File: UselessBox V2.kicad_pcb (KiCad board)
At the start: 2 copper layers, 47.1 x 46.6 mm, 23 parts, among them J2 Conn_01x03, J3 Conn_01x02_Female, SW1 SW_SPDT, SW2 SW_SPDT, U1 L7805CV, U2 LM555CN_NOPB

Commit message: corrected power switch location
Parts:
- removed G***: LOGO, Kicad:TNT Logo 12.6mm x 7mm
- removed G***: LOGO, Kicad:TSL Technologies logo 16mm x 11mm
- R3: value 82KΩ -> 100KΩ
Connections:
- D5 pad 2: /5Vout -> /5V
- J2 pad 2: /5Vout -> /5V
- J3 pad 2: /B+ -> Net-(J3-Pad2)
- R2 pad 1: /5Vout -> /5V
- R3 pad 1: /5Vout -> /5V
- SW1 pad 1: /5Vout -> /B+
- SW1 pad 2: /5V -> Net-(J3-Pad2)
- U2 pad 4: /5Vout -> /5V
- U2 pad 8: /5Vout -> /5V
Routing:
- net /5Vout: track 157.8 -> 0.00 mm
- net /5V: track 51.6 -> 125.9 mm
- net Net-(J3-Pad2): track 0.00 -> 43.0 mm
- net /B+: track 33.0 -> 48.2 mm
- net /B-: track 38.4 -> 44.0 mm
- added copper zone on F.Cu, net /5V
- removed copper zone on F.Cu, net /5Vout

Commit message: stl file done for base and arm also revised PCB switch
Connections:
- net /5V renamed /5Vout
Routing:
- net /GND: track 16.4 -> 78.0 mm
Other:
- board text added: "Useless Box V2 Timothy S Leishman 4/25/2022"
- board text removed: "Useless Box V2 Timothy S Leishman 4/12/2022"

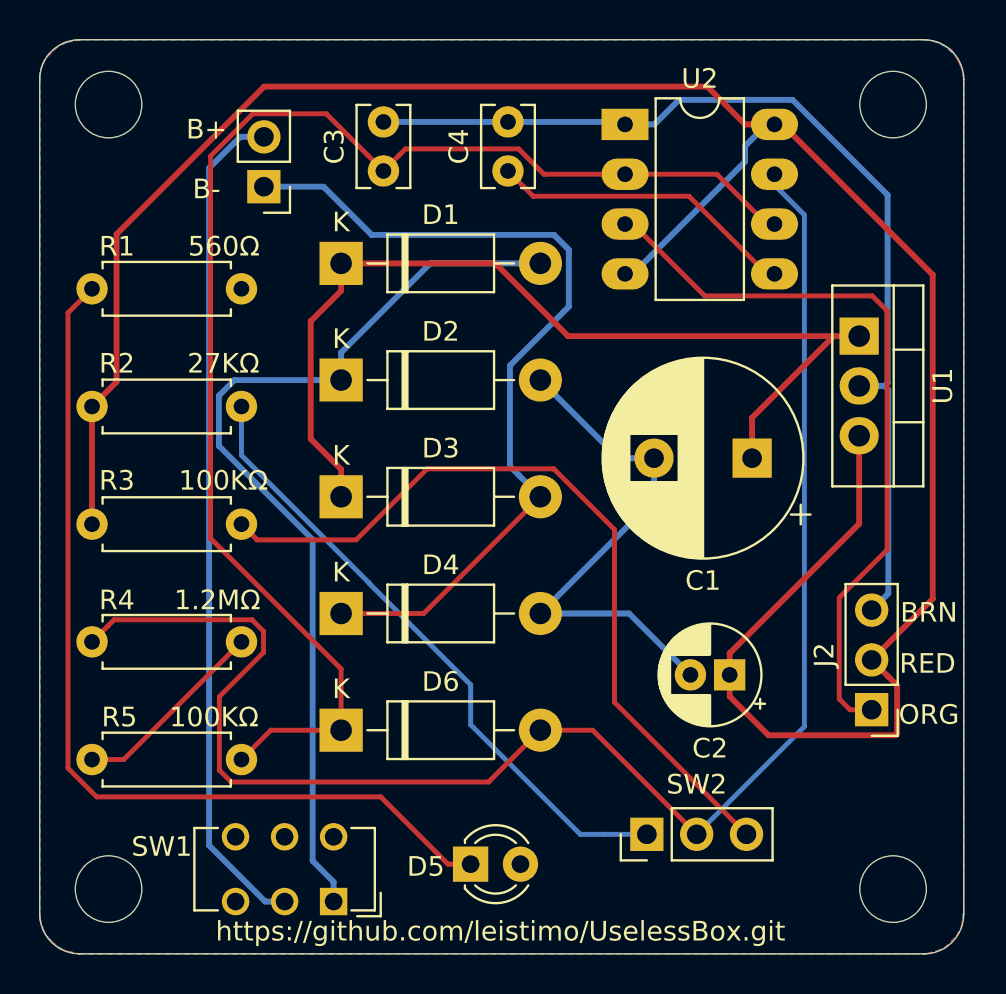
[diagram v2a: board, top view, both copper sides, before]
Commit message: Corrected ground problem and generated Gerbers
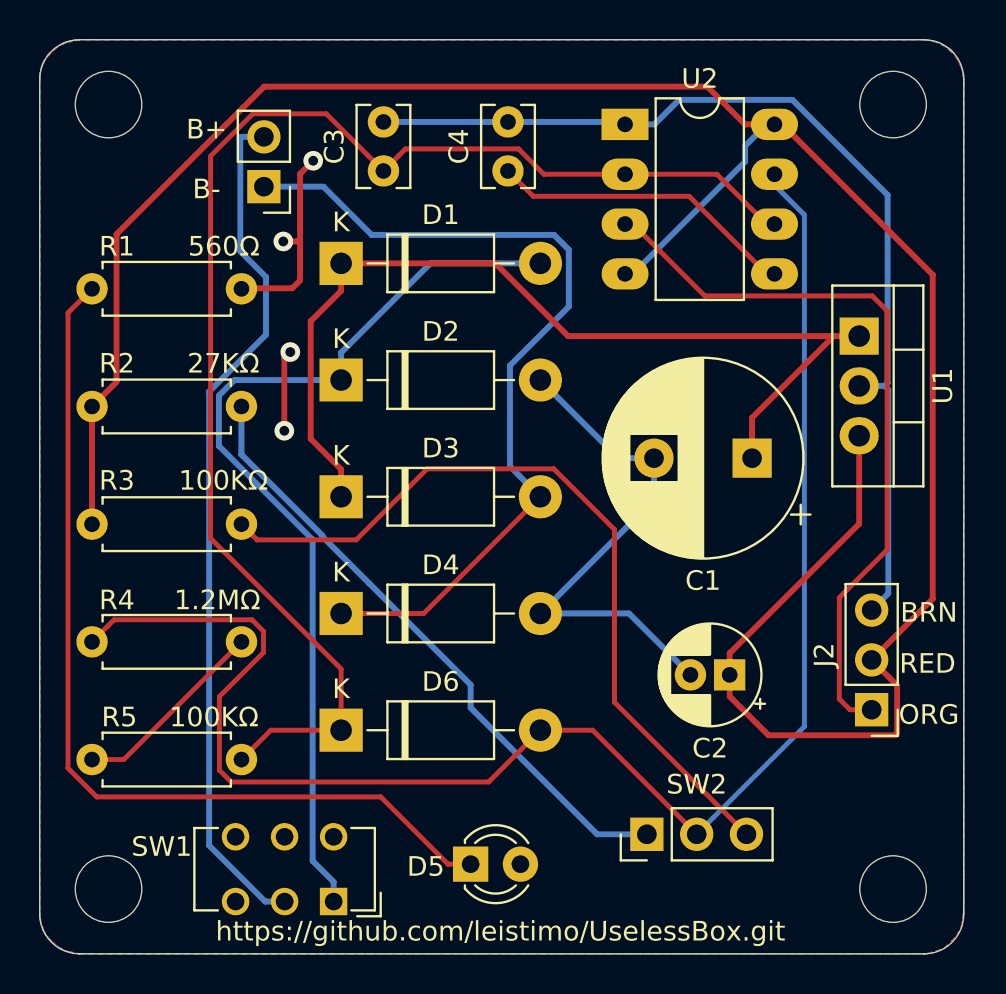
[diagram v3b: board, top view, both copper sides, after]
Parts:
- added G***: LOGO, Kicad:TSL Technologies logo 16mm x 11mm, B.Cu at (144.9, 113.0)
- added G***: LOGO, Kicad:TNT Logo 12.6mm x 7mm, B.Cu at (158.5, 104.8)
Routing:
- net /GND: track 78.0 -> 92.6 mm, vias 0 -> 4
- net Net-(J3-Pad2): track 43.0 -> 44.1 mm

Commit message: Version 3
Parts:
- removed C4: 0.022uF, Capacitor_THT:C_Rect_L4.0mm_W2.5mm_P2.50mm
- removed D3, D4, D6: D_Small_ALT, Diode_THT:D_DO-41_SOD81_P10.16mm_Horizontal
- removed D5: LED_GRN, LED_THT:LED_D3.0mm
- removed G***: LOGO, Kicad:TSL Technologies logo 16mm x 11mm
- removed G***: LOGO, Kicad:TNT Logo 12.6mm x 7mm
- removed SW2: SW_SPDT, Connector_PinHeader_2.54mm:PinHeader_1x03_P2.54mm_Vertical
- removed U2: LM555CN_NOPB, Package_DIP:DIP-8_W7.62mm_LongPads
- added J1: Conn_01x02_Female, Connector_PinHeader_2.54mm:PinHeader_1x02_P2.54mm_Vertical, F.Cu at (148.4, 118.7)
- added REF**: TSLsmall, TSL_Logos:TSLsmall, F.Cu at (129.2, 108.1)
- added REF**: BennySmall, TSL_Logos:BennySmall, F.Cu at (129.9, 94.1)
- added REF**: BennySmall, TSL_Logos:BennySmall, B.Cu at (129.8, 108.8)
- added REF**: TSLsmall, TSL_Logos:TSLsmall, B.Cu at (129.2, 93.9)
- C1: value 470uF -> 47uF; footprint Capacitor_THT:CP_Radial_D10.0mm_P5.00mm -> Capacitor_THT:CP_Radial_D5.0mm_P2.00mm
- C2: value 47uF -> 0.022uF; footprint Capacitor_THT:CP_Radial_D5.0mm_P2.00mm -> Capacitor_THT:C_Rect_L4.0mm_W2.5mm_P2.50mm
- D1: value D_Small_ALT -> LED_GRN; footprint Diode_THT:D_DO-41_SOD81_P10.16mm_Horizontal -> LED_THT:LED_D3.0mm
- J2: value Conn_01x03 -> Switch; footprint Connector_PinHeader_2.54mm:PinHeader_1x03_P2.54mm_Vertical -> Connector_JST:JST_VH_B2P-VH-FB-B_1x02_P3.96mm_Vertical
- J3: value Conn_01x02_Female -> Conn_01x03; footprint Connector_PinHeader_2.54mm:PinHeader_1x02_P2.54mm_Vertical -> Connector_PinHeader_2.54mm:PinHeader_1x03_P2.54mm_Vertical
- SW1: footprint Button_Switch_THT:SW_CuK_JS202011CQN_DPDT_Straight -> Connector_PinHeader_2.54mm:PinHeader_1x03_P2.54mm_Vertical
- U1: value L7805CV -> LM555CN_NOPB; footprint Package_TO_SOT_THT:TO-220-3_Vertical -> Package_DIP:DIP-8_W7.62mm_LongPads
- moved SW1 28.1 mm to (161.0, 104.0), turned to 0 degrees
- moved C3 27.2 mm to (148.7, 110.9), turned to 0 degrees
- moved J3 26.3 mm to (161.0, 92.5), turned to 0 degrees
- moved D2 24.0 mm to (143.8, 118.9), turned to 180 degrees
- moved U1 19.4 mm to (146.8, 91.2), turned to 0 degrees
- moved R1 15.9 mm to (141.2, 83.4), turned to 180 degrees
- moved C1 15.2 mm to (159.1, 84.1), turned to 0 degrees
- moved J2 12.0 mm to (156.5, 118.2), turned to 0 degrees
- moved C2 11.6 mm to (148.8, 105.9), turned to 0 degrees
- moved D1 10.5 mm to (148.5, 83.4)
- moved R2 8.86 mm to (133.6, 90.6)
- moved R3 8.11 mm to (133.6, 97.9)
- moved R4 7.47 mm to (133.6, 105.1)
- moved R5 6.99 mm to (133.6, 112.3)
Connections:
- C2 pad 1: /5Vout -> Net-(D2-K)
- C3 pad 1: Net-(C3-Pad1) -> Net-(U1-CONT)
- D1 pad 1: /VIN+ -> Net-(D1-K)
- D1 pad 2: /B+ -> /VIN+
- D2 pad 1: /B+ -> Net-(D2-K)
- D2 pad 2: /GND -> Net-(D2-A)
- J2 pad 1: Net-(J2-Pad1) -> /B+
- J2 pad 2: /5Vout -> /VIN+
- J3 pad 1: /B- -> Net-(J3-Pin_1)
- J3 pad 2: Net-(J3-Pad2) -> /VIN+
- R1 pad 1: Net-(D5-Pad1) -> Net-(D1-K)
- R2 pad 1: /5Vout -> /VIN+
- R2 pad 2: Net-(R2-Pad2) -> Net-(SW1-A)
- R3 pad 1: /5Vout -> /VIN+
- R3 pad 2: Net-(R3-Pad2) -> Net-(SW1-C)
- R4 pad 1: Net-(D6-Pad2) -> Net-(D2-A)
- R5 pad 2: Net-(C3-Pad1) -> Net-(D2-K)
- SW1 pad 1: /B+ -> Net-(SW1-A)
- SW1 pad 2: Net-(J3-Pad2) -> Net-(D2-A)
- SW1 pad 3: (no net) -> Net-(SW1-C)
- U1 pad 1: /VIN+ -> /GND
- U1 pad 2: /GND -> Net-(D2-K)
- U1 pad 3: /5Vout -> Net-(J3-Pin_1)
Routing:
- net /5Vout: track 125.9 -> 0.00 mm
- net /GND: track 92.6 -> 0.00 mm, vias 4 -> 0
- net Net-(D6-Pad2): track 81.9 -> 0.00 mm
- net Net-(C3-Pad1): track 71.0 -> 0.00 mm
- net Net-(SW1-C): track 0.00 -> 66.6 mm
- net Net-(D2-A): track 0.00 -> 60.6 mm
- net /VIN+: track 49.1 -> 0.00 mm
- net Net-(D5-Pad1): track 47.5 -> 0.00 mm
- net Net-(J3-Pad2): track 44.1 -> 0.00 mm
- net /B-: track 44.0 -> 0.00 mm
- net Net-(D2-K): track 0.00 -> 43.8 mm
- net Net-(R3-Pad2): track 40.5 -> 0.00 mm
- net /B+: track 48.2 -> 10.1 mm
- net Net-(J2-Pad1): track 37.9 -> 0.00 mm
- net Net-(R2-Pad2): track 31.9 -> 0.00 mm
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- added copper zone on F.Cu, net /VIN+
- removed copper zone on F.Cu, net /5Vout
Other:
- net class Default removed
- net class Power removed
- board text added: "O+"
- board text added: "O-"
- board text added: "Power Switch"
- board text added: "Useless Box V3 Timothy S Leishman 2025"
- board text removed: "B+"
- board text removed: "B-"
- board text removed: "Useless Box V2 Timothy S Leishman 4/25/2022"
- board text removed: "https://github.com/leistimo/UselessBox.git"
